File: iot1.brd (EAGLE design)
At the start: 160 x 100 mm, 35 parts, among them IC1 MEGA8-P, IC2 7805T, IC3 LTC2486C, J1 DCJ0202, U2 HTU21D, X1 22-23-2041, X2 A1944-50

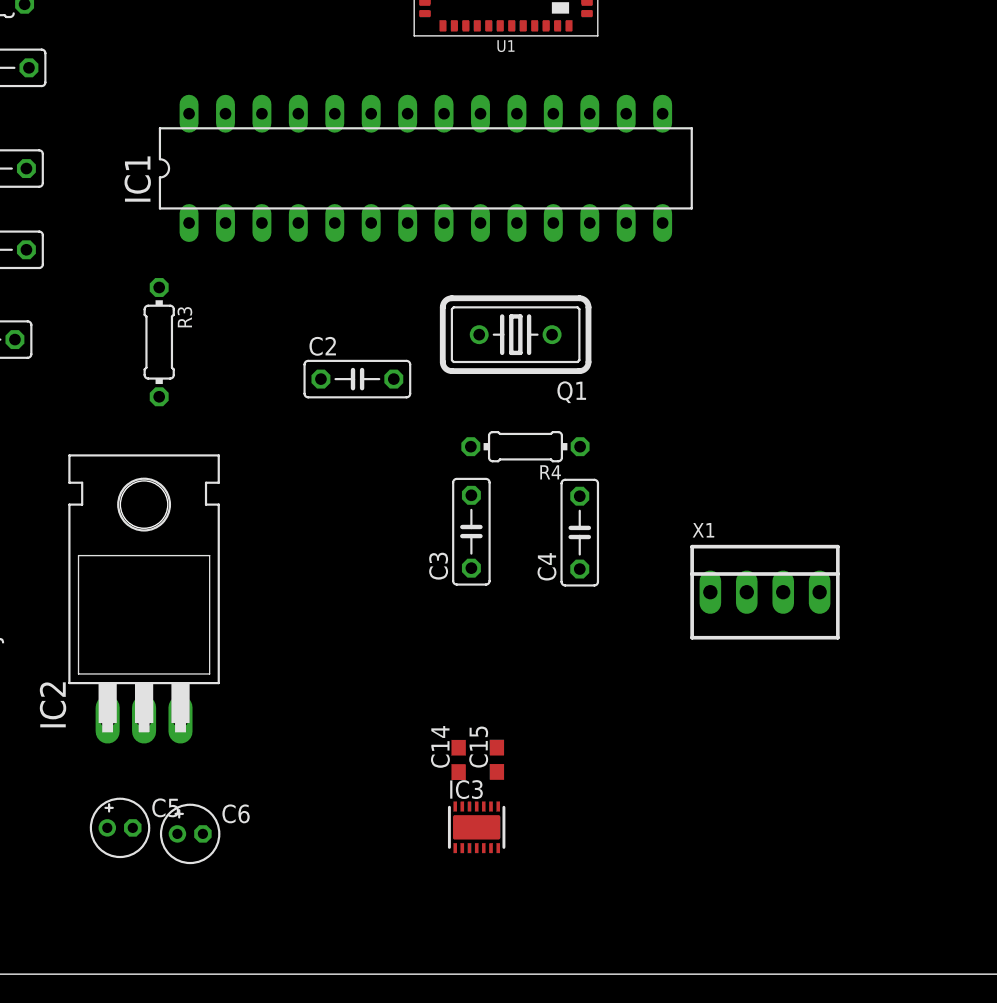
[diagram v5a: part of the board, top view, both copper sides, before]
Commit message: 3.3V regulator, multiplexer
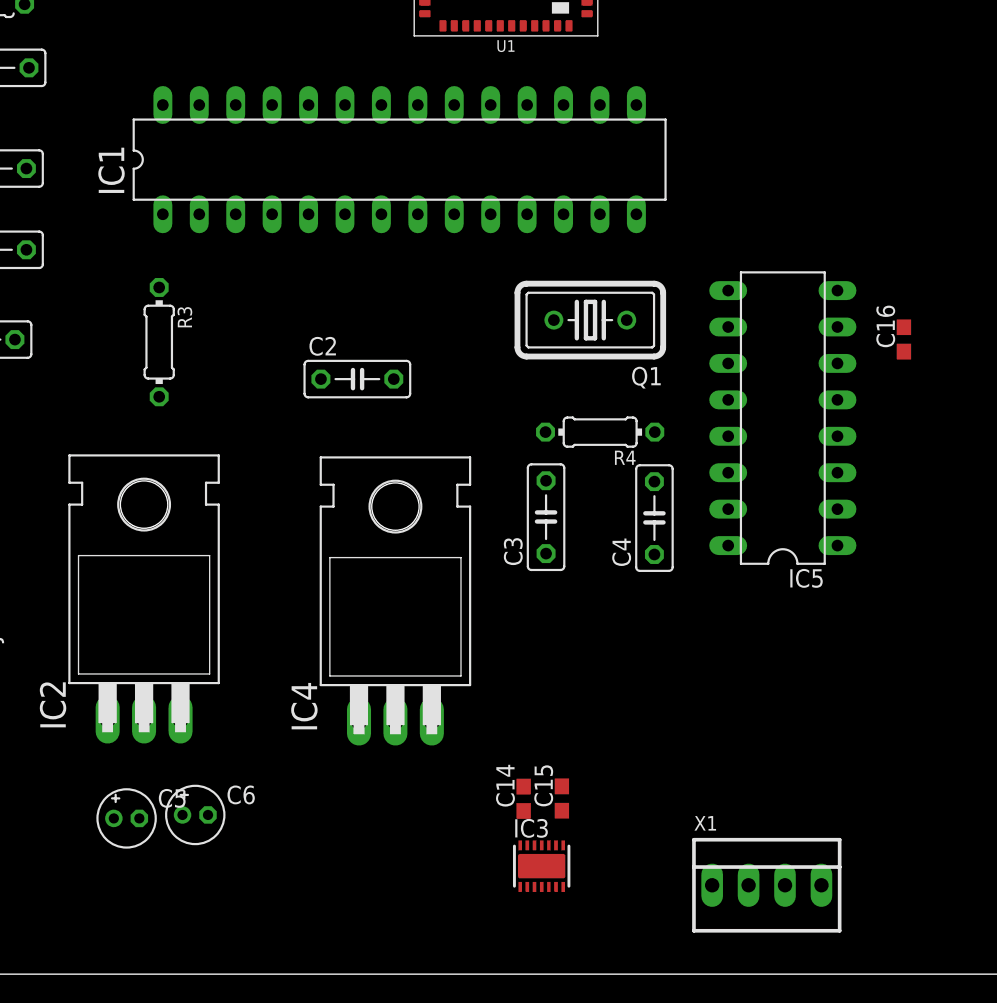
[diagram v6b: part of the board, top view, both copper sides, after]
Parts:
- added C16: (no value), rcl:C0603
- added IC4: 7805T, linear:TO220H
- added IC5: 4051N, 40xx:DIL16
- moved X1 20.4 mm to (66.8, 6.20)
- moved C3 5.31 mm to (51.4, 31.9)
- moved C4 5.31 mm to (58.9, 31.8)
- moved R4 5.31 mm to (55.1, 37.8)
- moved Q1 5.31 mm to (54.4, 45.6)
- moved C14 5.28 mm to (49.8, 12.2)
- moved C15 5.28 mm to (52.5, 12.2)
- moved IC3 5.28 mm to (51.1, 7.53)
- moved IC1 1.93 mm to (41.1, 56.8)
- moved C6 1.37 mm to (26.9, 11.1)
- moved C5 0.80 mm to (22.1, 10.9)
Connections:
- net 3.3V: now also IC4.3
- net 5V: now also C16.1, IC4.1, IC5.16
- net GND: now also C16.2, IC4.2, IC5.7, IC5.8

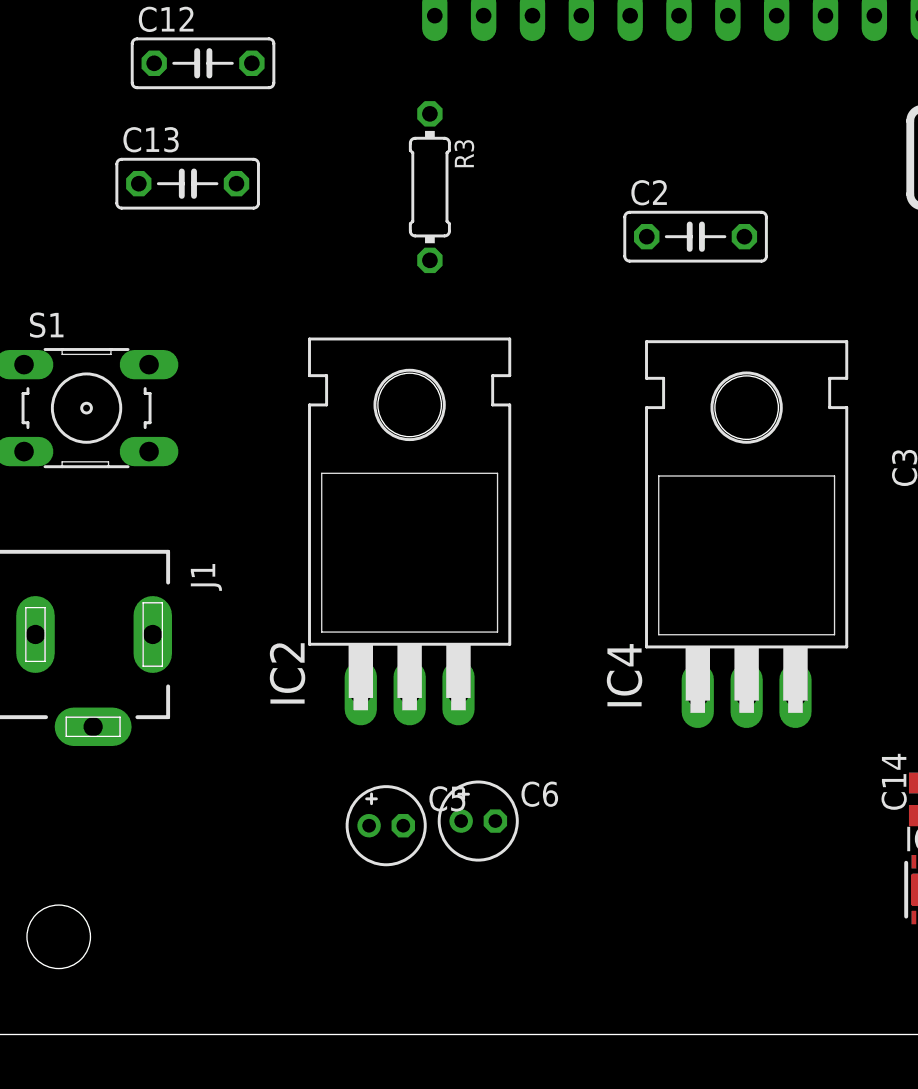
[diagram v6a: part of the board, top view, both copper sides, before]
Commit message: 1Hz filter
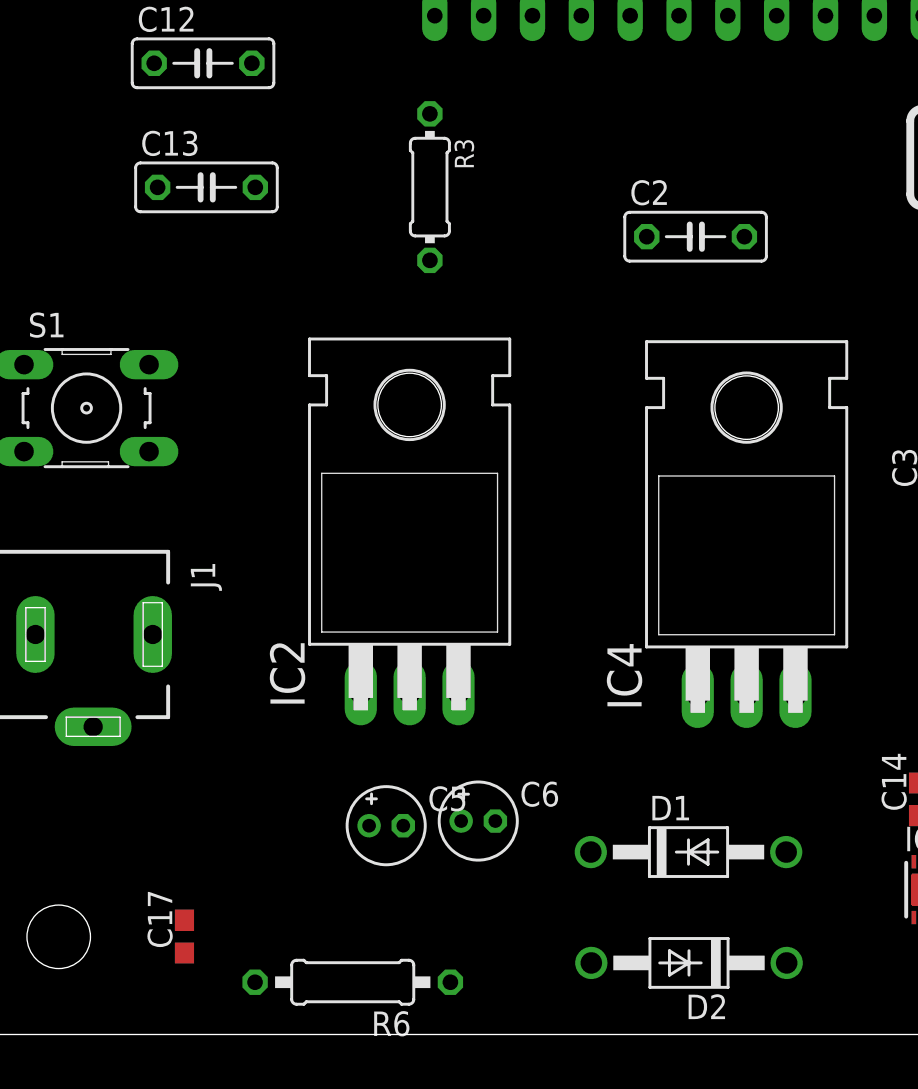
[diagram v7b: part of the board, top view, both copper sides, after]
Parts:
- added C17: (no value), rcl:C0603
- added D1, D2: 1N4004, diode:DO41-10
- added R6: (no value), rcl:0207/10
- moved C13 1.00 mm to (12.8, 44.1)
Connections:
- removed net N$76: IC3.8
- new net MUX_0: IC5.11
- new net MUX_1: IC5.10
- new net MUX_2: IC5.9
- new net N$29: IC5.12
- new net N$36: IC5.1
- new net N$50: IC5.5
- new net N$65: IC5.2
- new net N$66: IC5.4
- new net N$9: IC5.15
- new net S: D1.A, D2.C, IC5.3, R6.1
- new net SENSORS: C17.1, IC3.8, R6.2
- net 5V: now also D1.C
- net GND: now also C17.2, D2.A, IC5.6
- net SOIL_MOISTURE_0: now also IC5.13
- net SOIL_MOISTURE_1: now also IC5.14

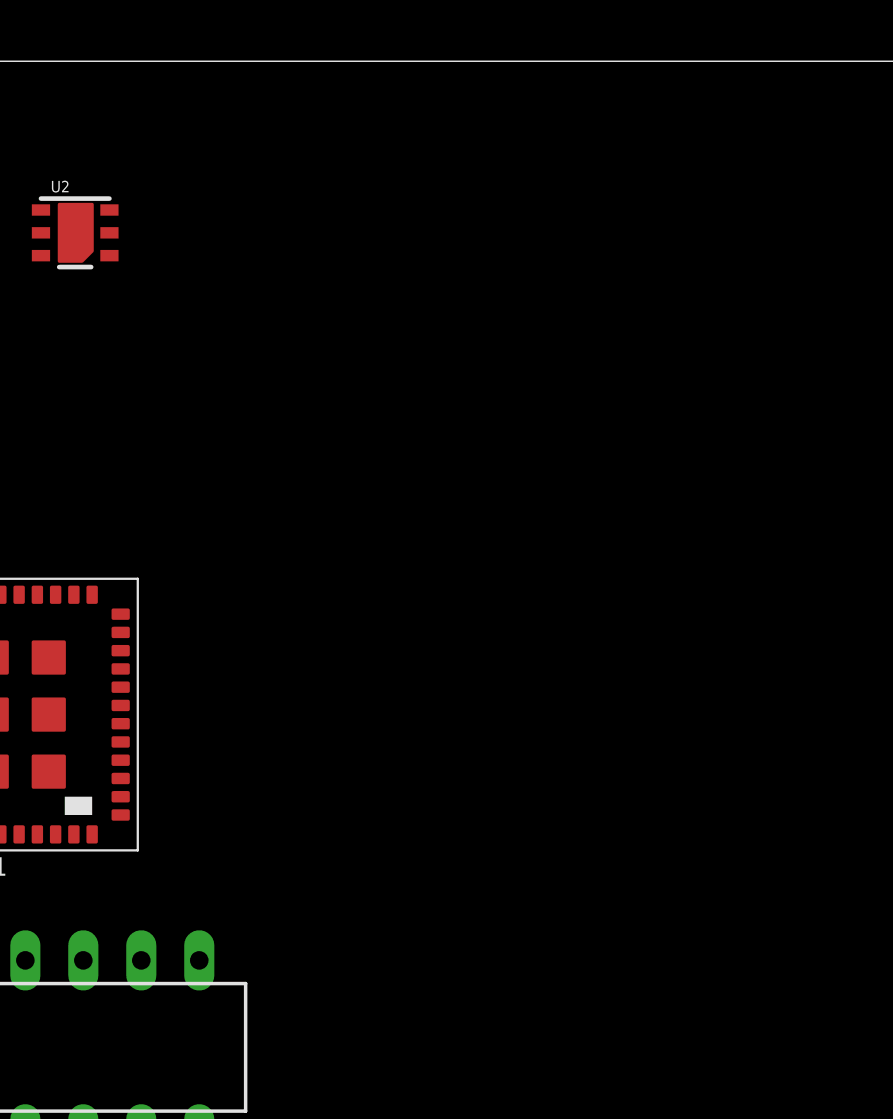
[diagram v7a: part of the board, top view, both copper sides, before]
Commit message: 4-20ma amplification for soil moisture sensors
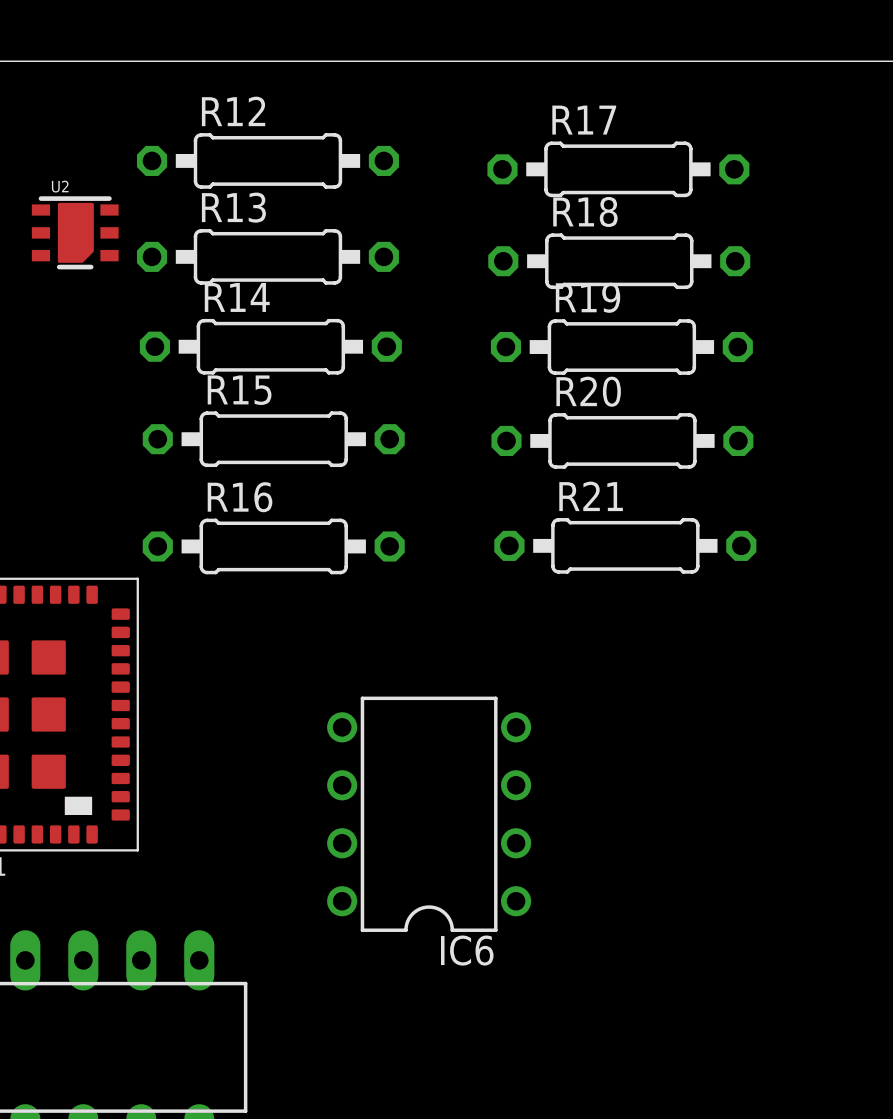
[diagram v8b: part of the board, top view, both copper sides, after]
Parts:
- added IC6: OPA2134PA, linear:DIL08
- added R12, R13, R14, R15, R16, R17, R18, R19, R20, R21: (no value), rcl:0207/10
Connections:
- new net N$78: IC6.3, R12.1, R16.2
- new net N$81: IC6.2, R14.2
- new net N$82: IC6.5, R20.1, R21.2
- new net N$83: IC6.6, R18.2
- new net SOIL_MOISTURE_AMPLIFIED_0: IC5.13, IC6.1, R12.2, R13.2
- new net SOIL_MOISTURE_AMPLIFIED_1: IC5.14, IC6.7, R19.2, R20.2
- net 5V: now also IC6.8, R15.1, R17.1
- net GND: now also IC6.4, R16.1, R21.1
- net SOIL_MOISTURE_0: now also R13.1, R14.1, R15.2; no longer IC5.13
- net SOIL_MOISTURE_1: now also R17.2, R18.1, R19.1; no longer IC5.14
